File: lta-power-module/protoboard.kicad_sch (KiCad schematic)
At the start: 224 parts

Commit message: Small sheet cleanup.
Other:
- note added: "${REV_DATE}"
- note added: "${REV}"
- note added: "Expansion protoboard"
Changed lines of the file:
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@@
     (stroke (width 0) (type default) (color 0 0 0 0))
+  )
+  (text "Expansion protoboard" (at 186.69 190.5 0)
+    (effects (font (size 1.27 1.27)) (justify left bottom))
+  )
+  (text "${REV}\n" (at 268.605 194.31 0)
+    (effects (font (size 1.27 1.27)) (justify left bottom))
   )
   (text "Flexible expansion protoboard" (at 186.69 174.625 0)
     (effects (font (size 2.54 2.54)) (justify left bottom))
   )
+  (text "${REV_DATE}" (at 207.01 194.31 0)
+    (effects (font (size 1.27 1.27)) (justify left bottom))
+  )
   (hierarchical_label "Vcc1" (shape input) (at 19.05 19.685 90)

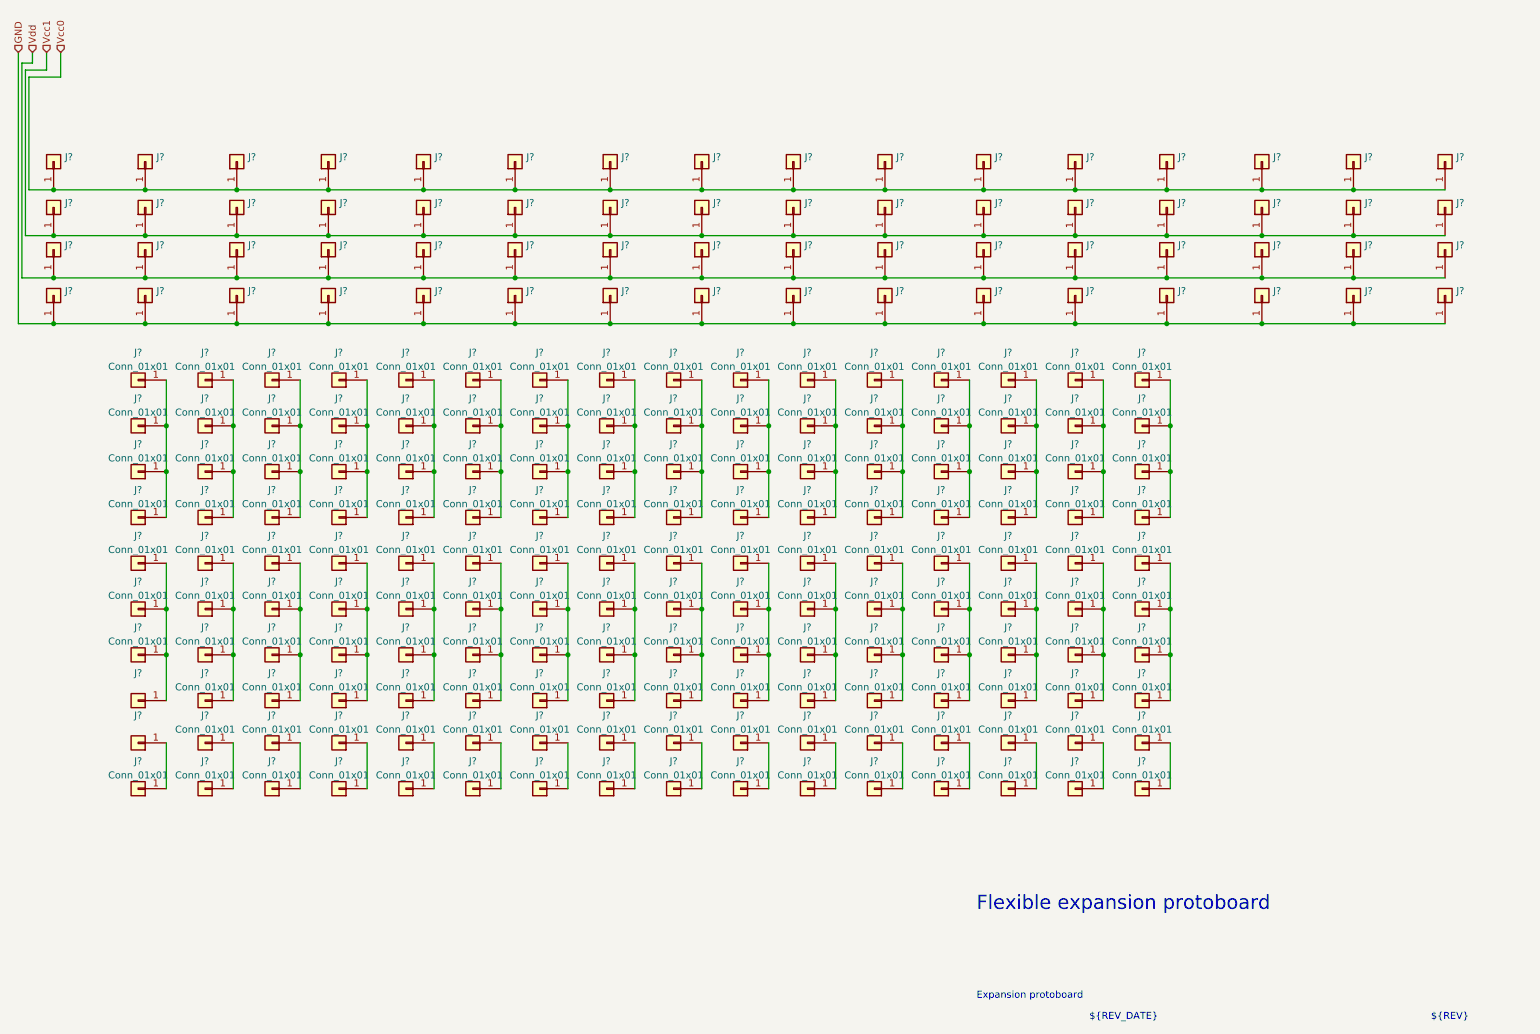
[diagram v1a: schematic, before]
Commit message: Add custom footprints for 12V regulator and power distribution bus.
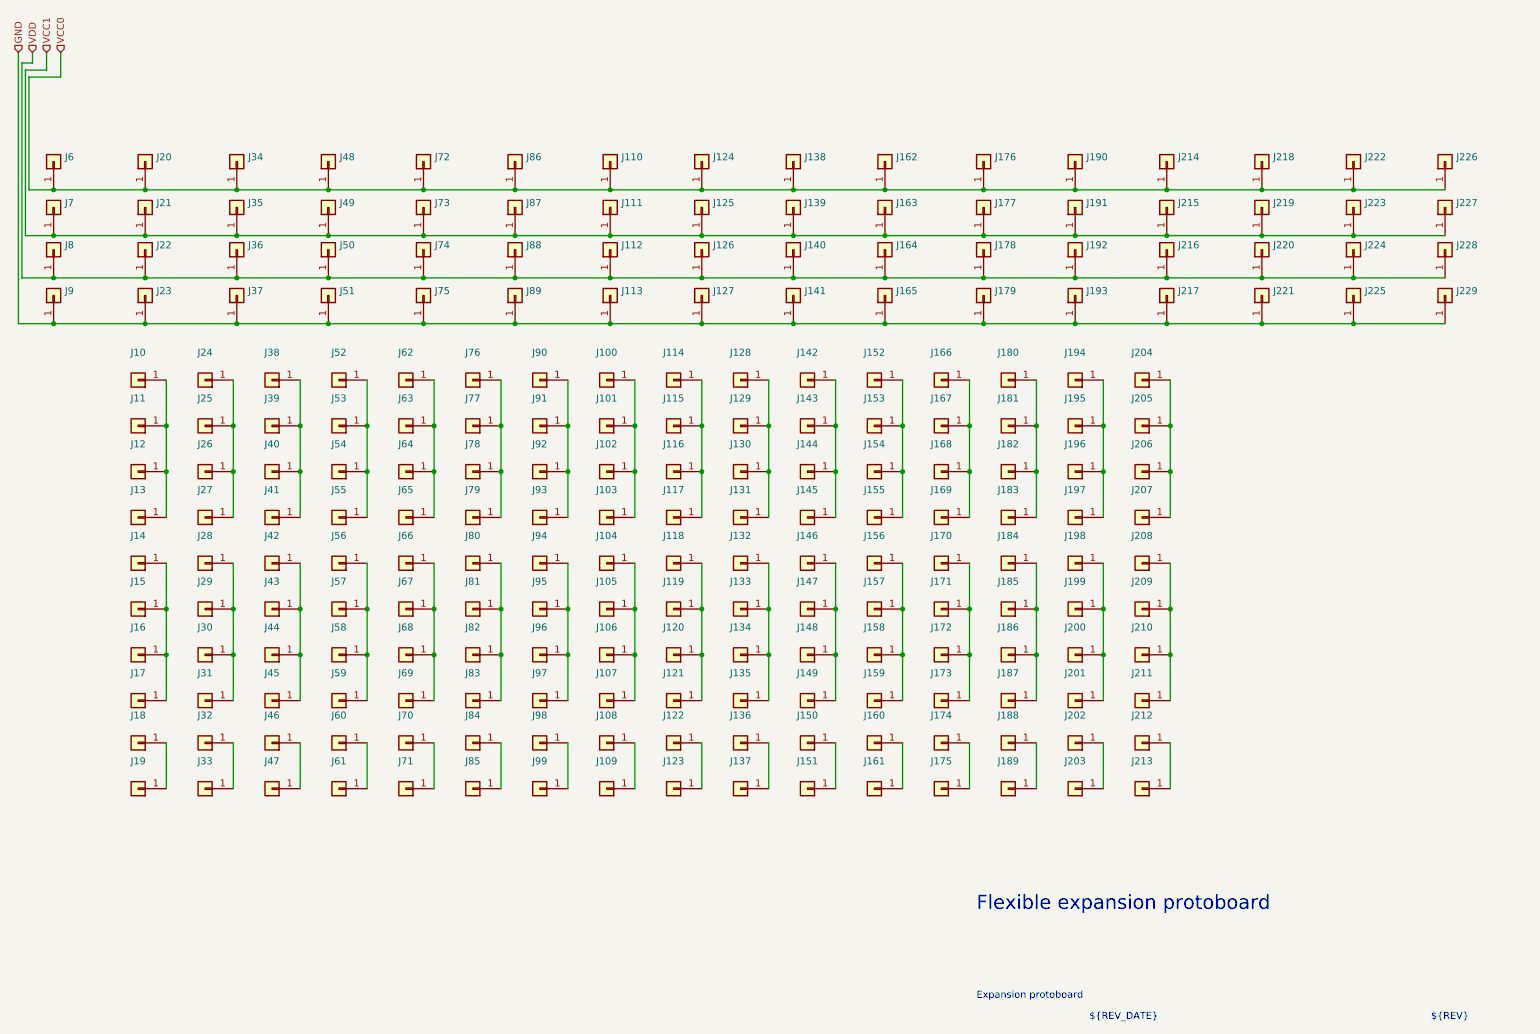
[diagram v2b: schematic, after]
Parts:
- J10, J100, J101, J102, J103, J104, J105, J106, J109, J11, J114, J115, J116, J117, J118, J119, J12, J120, J123, J128, J129, J13, J130, J131, J132, J133, J134, J137, J14, J142, J143, J144, J145, J146, J147, J148, J15, J151, J152, J153, J154, J155, J156, J157, J158, J16, J161, J166, J167, J168, J169, J170, J171, J172, J175, J180, J181, J182, J183, J184, J185, J186, J189, J19, J194, J195, J196, J197, J198, J199, J200, J203, J204, J205, J206, J207, J208, J209, J210, J213, J24, J25, J26, J27, J28, J29, J30, J33, J38, J39, J40, J41, J42, J43, J44, J47, J52, J53, J54, J55, J56, J57, J58, J61, J62, J63, J64, J65, J66, J67, J68, J71, J76, J77, J78, J79, J80, J81, J82, J85, J90, J91, J92, J93, J94, J95, J96, J99: renamed from J?; value Conn_01x01 -> (none); footprint Aaron_Pads:1mm_PTH_No_Silk -> (none)
- J107, J108, J121, J122, J135, J136, J149, J150, J159, J160, J173, J174, J187, J188, J201, J202, J211, J212, J31, J32, J45, J46, J59, J60, J69, J70, J83, J84, J97, J98: renamed from J?; value Conn_01x01 -> (none); footprint Aaron_Pads:1.6mm_PTH_No_Silk -> (none)
- gave numbers to parts that had none: 66
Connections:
- net Vcc0 renamed VCC0
- net Vcc1 renamed VCC1
- net Vdd renamed VDD

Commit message: Remove unnecessary LEDs.
The MOSFET drivers have LEDs which will operate based on the gate
signal alone; we can just rely on those.
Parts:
- J10, J100, J101, J102, J103, J104, J105, J106, J109, J11, J110, J111, J112, J113, J114, J115, J116, J117, J118, J119, J12, J120, J123, J124, J125, J126, J127, J128, J129, J13, J130, J131, J132, J133, J134, J137, J138, J139, J14, J140, J141, J142, J143, J144, J145, J146, J147, J148, J15, J151, J152, J153, J154, J155, J156, J157, J158, J16, J161, J162, J163, J164, J165, J166, J167, J168, J169, J170, J171, J172, J175, J176, J177, J178, J179, J180, J181, J182, J183, J184, J185, J186, J189, J19, J190, J191, J192, J193, J194, J195, J196, J197, J198, J199, J20, J200, J203, J204, J205, J206, J207, J208, J209, J21, J210, J213, J214, J215, J216, J217, J218, J219, J22, J220, J221, J222, J223, J224, J225, J226, J227, J228, J229, J23, J24, J25, J26, J27, J28, J29, J30, J33, J34, J35, J36, J37, J38, J39, J40, J41, J42, J43, J44, J47, J48, J49, J50, J51, J52, J53, J54, J55, J56, J57, J58, J6, J61, J62, J63, J64, J65, J66, J67, J68, J7, J71, J72, J73, J74, J75, J76, J77, J78, J79, J8, J80, J81, J82, J85, J86, J87, J88, J89, J9, J90, J91, J92, J93, J94, J95, J96, J99: Comment (none) -> standard 1mm PTH for prototyping
- J107, J108, J121, J122, J135, J136, J149, J150, J159, J160, J17, J173, J174, J18, J187, J188, J201, J202, J211, J212, J31, J32, J45, J46, J59, J60, J69, J70, J83, J84, J97, J98: Comment (none) -> larger 1.6mm holes for DO201 diodes, larger capacitors

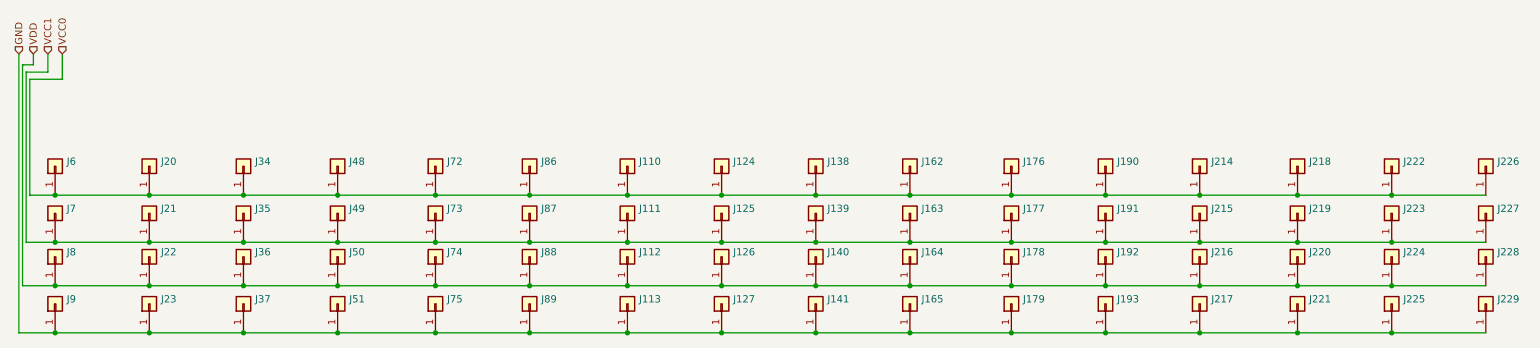
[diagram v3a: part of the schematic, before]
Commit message: Considerably more work on power module PCB.
* Slight reorganization of layout.
* Routed all traces.
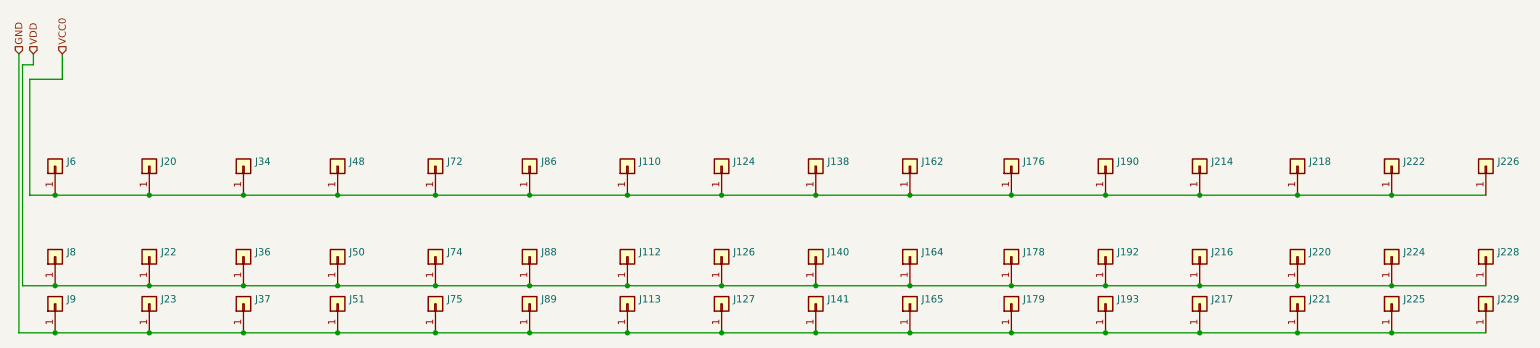
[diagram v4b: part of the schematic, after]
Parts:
- removed J111, J125, J139, J163, J177, J191, J21, J215, J219, J223, J227, J35, J49, J7, J73, J87: (no value), symbol Connector_Generic:Conn_01x01

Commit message: Add protoboard.
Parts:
- removed J136, J137, J150, J151, J174, J175, J188, J189, J202, J203, J212, J213, J32, J33, J84, J85: (no value), symbol Connector_Generic:Conn_01x01
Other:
- moved on the sheet: J108, J109, J122, J123, J160, J161, J46, J47, J60, J61, J70, J71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

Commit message: Work on border.
* Add perimeter edge cut to fit WH-22 polycase.
* Add M5 mounting holes in temp locations on PCB.
* Lay out and lock left-edge M5 mounting holes.
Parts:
- J107, J121, J135, J149, J159, J17, J173, J187, J201, J211, J31, J45, J59, J69, J83, J97: Comment larger 1.6mm holes for DO201 diodes, larger capacitors -> standard 1mm PTH for prototyping
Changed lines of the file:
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@@
       (effects (font (size 1.27 1.27)) hide)
     )
-    (property "Comment" "larger 1.6mm holes for DO201 diodes, larger capacitors" (id 4) (at 192.405 136.525 0)
+    (property "Comment" "standard 1mm PTH for prototyping" (id 4) (at 192.405 136.525 0)
       (effects (font (size 1.27 1.27)) hide)
     )
@@
       (effects (font (size 1.27 1.27)) hide)
     )
-    (property "Comment" "larger 1.6mm holes for DO201 diodes, larger capacitors" (id 4) (at 35.56 136.525 0)
+    (property "Comment" "standard 1mm PTH for prototyping" (id 4) (at 35.56 136.525 0)
       (effects (font (size 1.27 1.27)) hide)
     )
@@
       (effects (font (size 1.27 1.27)) hide)
     )
-    (property "Comment" "larger 1.6mm holes for DO201 diodes, larger capacitors" (id 4) (at 47.625 136.525 0)
+    (property "Comment" "standard 1mm PTH for prototyping" (id 4) (at 47.625 136.525 0)
       (effects (font (size 1.27 1.27)) hide)
     )
@@
       (effects (font (size 1.27 1.27)) hide)
     )
-    (property "Comment" "larger 1.6mm holes for DO201 diodes, larger capacitors" (id 4) (at 107.95 136.525 0)
+    (property "Comment" "standard 1mm PTH for prototyping" (id 4) (at 107.95 136.525 0)
       (effects (font (size 1.27 1.27)) hide)
     )
@@
       (effects (font (size 1.27 1.27)) hide)
     )
-    (property "Comment" "larger 1.6mm holes for DO201 diodes, larger capacitors" (id 4) (at 95.885 136.525 0)
+    (property "Comment" "standard 1mm PTH for prototyping" (id 4) (at 95.885 136.525 0)
       (effects (font (size 1.27 1.27)) hide)
     )
@@
       (effects (font (size 1.27 1.27)) hide)
     )
-    (property "Comment" "larger 1.6mm holes for DO201 diodes, larger capacitors" (id 4) (at 168.275 136.525 0)
+    (property "Comment" "standard 1mm PTH for prototyping" (id 4) (at 168.275 136.525 0)
       (effects (font (size 1.27 1.27)) hide)
     )
@@
       (effects (font (size 1.27 1.27)) hide)
     )
-    (property "Comment" "larger 1.6mm holes for DO201 diodes, larger capacitors" (id 4) (at 59.69 136.525 0)
+    (property "Comment" "standard 1mm PTH for prototyping" (id 4) (at 59.69 136.525 0)
       (effects (font (size 1.27 1.27)) hide)
     )
@@
       (effects (font (size 1.27 1.27)) hide)
     )
-    (property "Comment" "larger 1.6mm holes for DO201 diodes, larger capacitors" (id 4) (at 204.47 136.525 0)
+    (property "Comment" "standard 1mm PTH for prototyping" (id 4) (at 204.47 136.525 0)
       (effects (font (size 1.27 1.27)) hide)
     )
@@
       (effects (font (size 1.27 1.27)) hide)
     )
-    (property "Comment" "larger 1.6mm holes for DO201 diodes, larger capacitors" (id 4) (at 216.535 136.525 0)
+    (property "Comment" "standard 1mm PTH for prototyping" (id 4) (at 216.535 136.525 0)
       (effects (font (size 1.27 1.27)) hide)
     )
@@
       (effects (font (size 1.27 1.27)) hide)
     )
-    (property "Comment" "larger 1.6mm holes for DO201 diodes, larger capacitors" (id 4) (at 144.145 136.525 0)
+    (property "Comment" "standard 1mm PTH for prototyping" (id 4) (at 144.145 136.525 0)
       (effects (font (size 1.27 1.27)) hide)
     )
@@
       (effects (font (size 1.27 1.27)) hide)
     )
-    (property "Comment" "larger 1.6mm holes for DO201 diodes, larger capacitors" (id 4) (at 132.08 136.525 0)
+    (property "Comment" "standard 1mm PTH for prototyping" (id 4) (at 132.08 136.525 0)
       (effects (font (size 1.27 1.27)) hide)
     )
@@
       (effects (font (size 1.27 1.27)) hide)
     )
-    (property "Comment" "larger 1.6mm holes for DO201 diodes, larger capacitors" (id 4) (at 71.755 136.525 0)
+    (property "Comment" "standard 1mm PTH for prototyping" (id 4) (at 71.755 136.525 0)
       (effects (font (size 1.27 1.27)) hide)
     )
@@
       (effects (font (size 1.27 1.27)) hide)
     )
-    (property "Comment" "larger 1.6mm holes for DO201 diodes, larger capacitors" (id 4) (at 180.34 136.525 0)
+    (property "Comment" "standard 1mm PTH for prototyping" (id 4) (at 180.34 136.525 0)
       (effects (font (size 1.27 1.27)) hide)
     )
@@
       (effects (font (size 1.27 1.27)) hide)
     )
-    (property "Comment" "larger 1.6mm holes for DO201 diodes, larger capacitors" (id 4) (at 120.015 136.525 0)
+    (property "Comment" "standard 1mm PTH for prototyping" (id 4) (at 120.015 136.525 0)
       (effects (font (size 1.27 1.27)) hide)
     )
@@
       (effects (font (size 1.27 1.27)) hide)
     )
-    (property "Comment" "larger 1.6mm holes for DO201 diodes, larger capacitors" (id 4) (at 83.82 136.525 0)
+    (property "Comment" "standard 1mm PTH for prototyping" (id 4) (at 83.82 136.525 0)
       (effects (font (size 1.27 1.27)) hide)
     )
@@
       (effects (font (size 1.27 1.27)) hide)
     )
-    (property "Comment" "larger 1.6mm holes for DO201 diodes, larger capacitors" (id 4) (at 156.21 136.525 0)
-      (effects (font (size 1.27 1.27)) hide)
-    )
+    (property "Comment" "standard 1mm PTH for prototyping" (id 4) (at 156.21 136.525 0)
+      (effects (font (size 1.27 1.27)) hide)
+    )
